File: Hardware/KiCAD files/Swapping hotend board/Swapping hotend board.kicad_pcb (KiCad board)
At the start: 2 copper layers, 3 parts, among them J19 PINHD_1x10_Male, J24 JST_SMD_1.0mm_Vertical

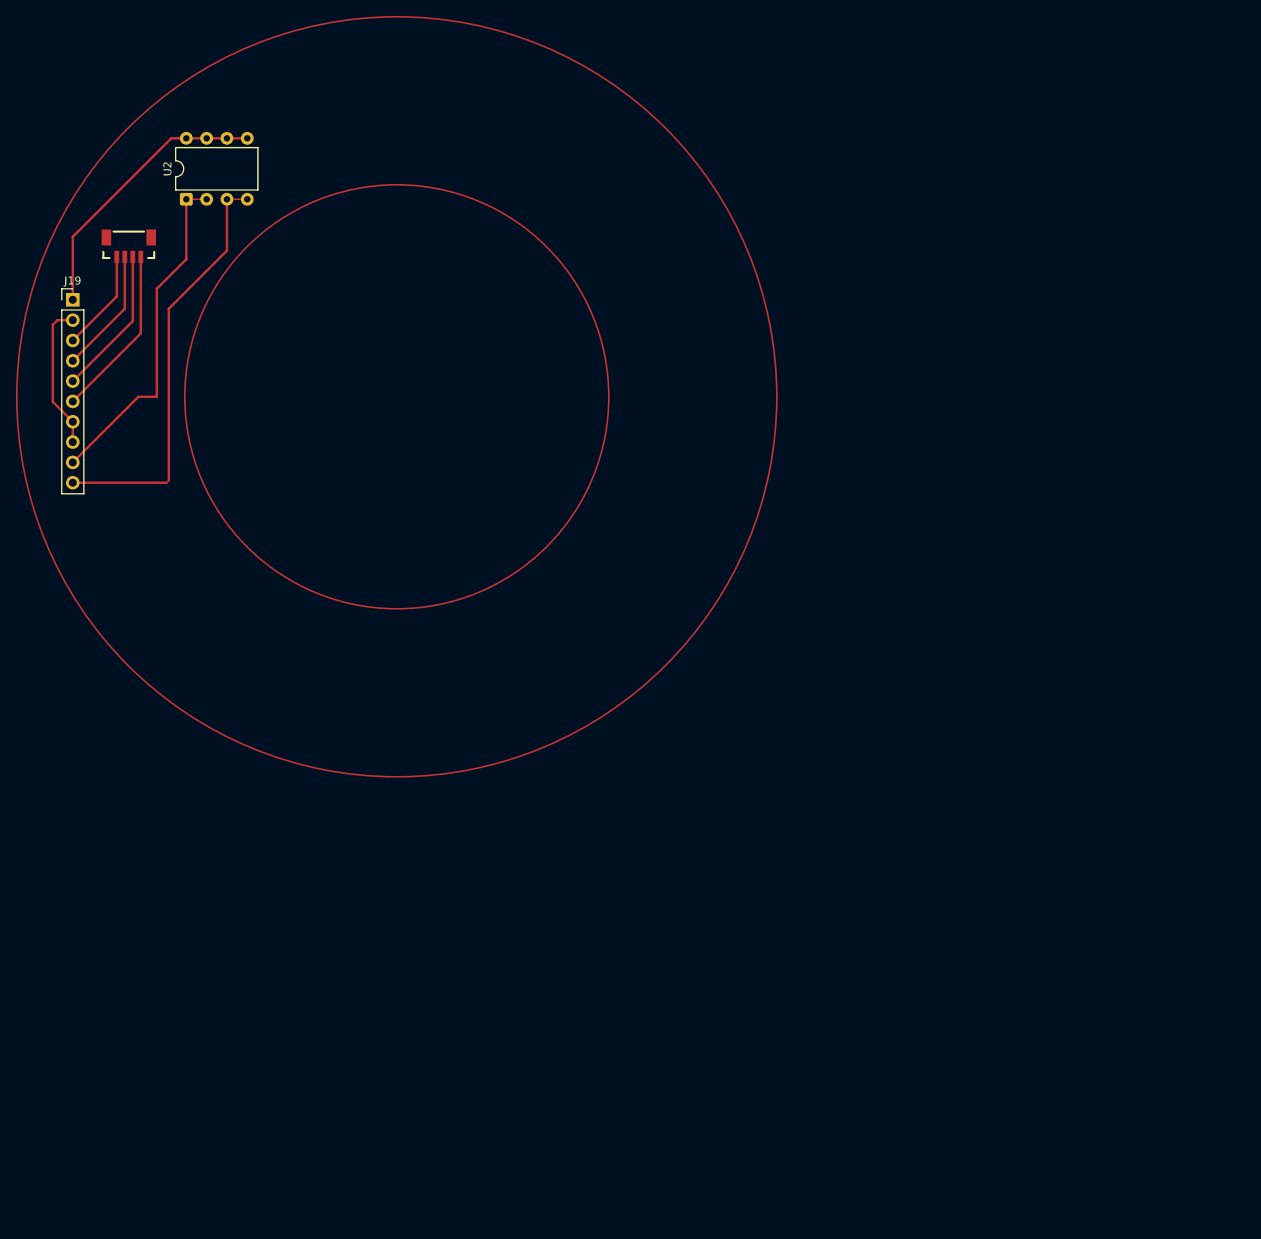
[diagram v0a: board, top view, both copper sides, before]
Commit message: Hotfix to create non-swapping board
hotfix on non-swapping done, swapping board is mapped for completion after CAD modeling phase begins
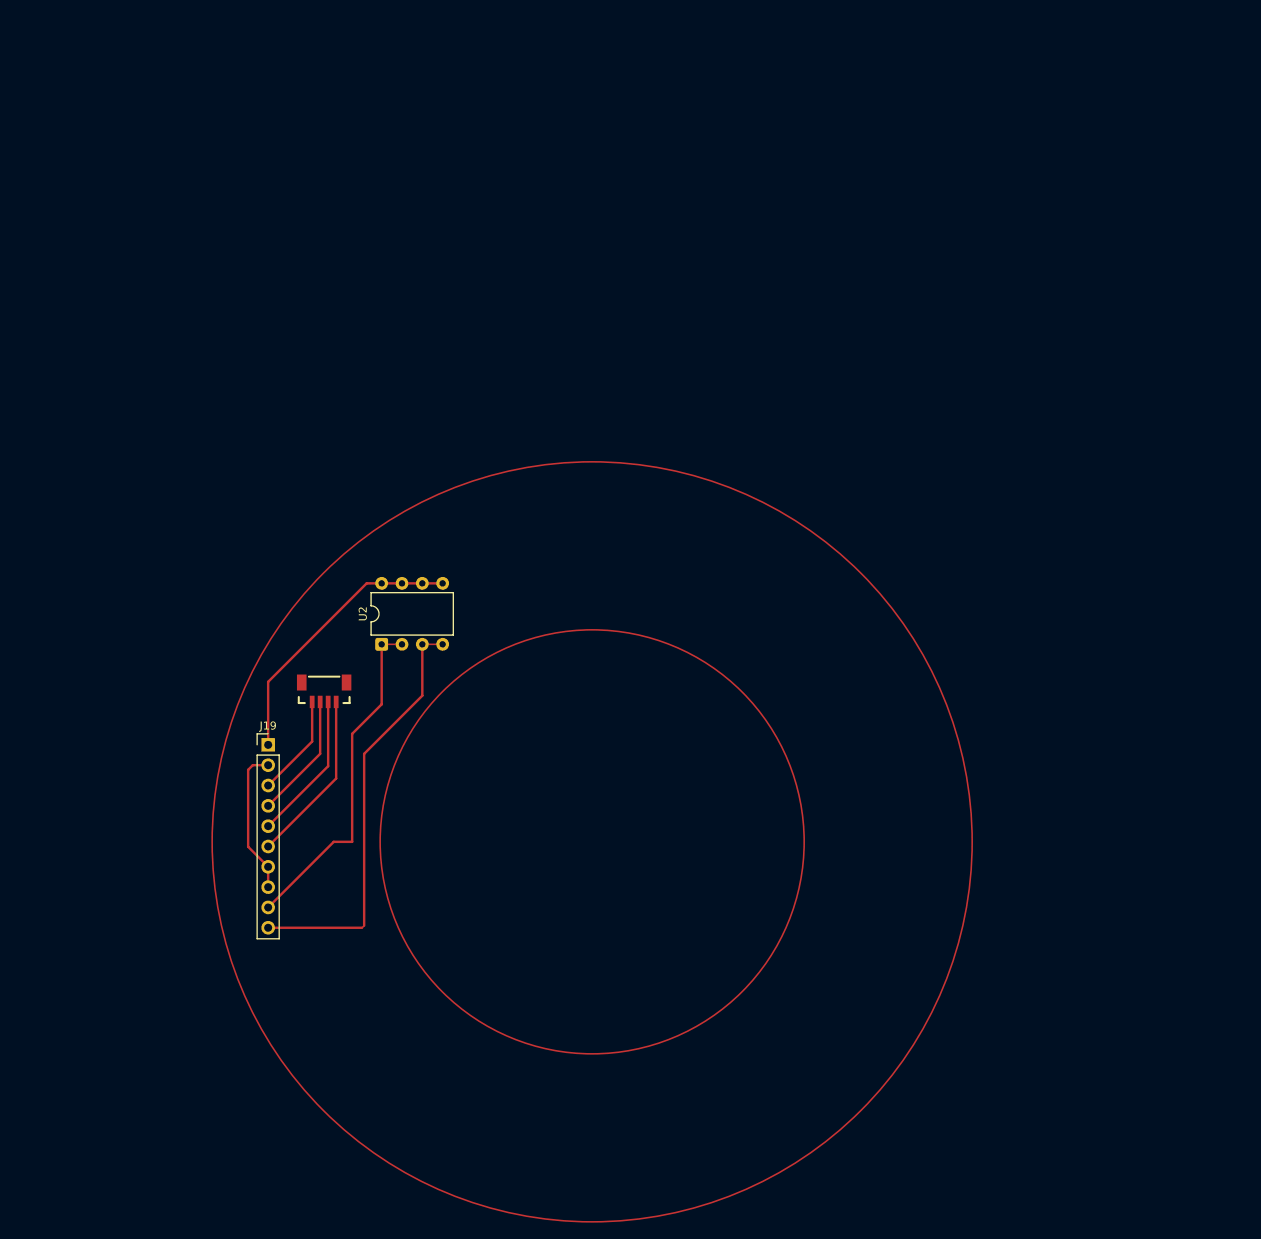
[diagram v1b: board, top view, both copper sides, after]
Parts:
- moved J19 60.8 mm to (46.4, 91.0)
- moved J24 60.8 mm to (53.4, 84.1)
- moved U2 60.8 mm to (60.6, 78.4)
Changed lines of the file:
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@@
 		(capping no)
 		(filling no)
-		(zone_defaults)
 		(pcbplotparams
 			(layerselection 0x00000000_00000000_55555555_5755f5ff)
@@
 	(footprint "Package_DIP:DIP-8_W7.62mm"
 		(layer "F.Cu")
-		(at 36.19 22.81 90)
+		(at 60.61 78.44 90)
 		(descr "8-lead though-hole mounted DIP package, row spacing 7.62mm (300 mils)")
 		(tags "THT DIP DIL PDIP 2.54mm 7.62mm 300mil")
@@
 		)
 		(point
-			(at 40 19)
+			(at 64.42 74.63)
 			(size 1.27)
 			(layer "F.Fab")
@@
 	(footprint "PCM_SparkFun-Connector:JST_1x04_P1.0mm_Vertical_SMD"
 		(layer "F.Cu")
-		(at 29 28.5)
+		(at 53.42 84.13)
 		(tags "SparkFun Qwiic Connector")
 		(property "Reference" "J24"
@@
 	(footprint "Connector_PinHeader_2.54mm:PinHeader_1x10_P2.54mm_Vertical"
 		(layer "F.Cu")
-		(at 22 35.38)
+		(at 46.42 91.01)
 		(descr "Through hole straight pin header, 1x10, 2.54mm pitch, single row")
 		(tags "Through hole pin header THT 1x10 2.54mm single row")
@@
 	)
 	(gr_circle
-		(center 62.5 47.5)
-		(end 89 47.31)
+		(center 86.92 103.13)
+		(end 113.42 102.94)
 		(stroke
 			(width 0.2)
@@
 	)
 	(gr_circle
-		(center 62.5 47.5)
-		(end 110 47.31)
+		(center 86.92 103.13)
+		(end 134.42 102.94)
 		(stroke
 			(width 0.2)
@@
 		(layer "F.Cu")
 		(pts
-			(xy 62.5 47.5) (xy 89.000681 47.5)
+			(xy 86.92 103.13) (xy 113.420681 103.13)
 		)
 		(height -51)
@@
 		)
 		(gr_text "26.5007"
-			(at 75.750341 -5.3 0)
+			(at 100.170341 50.33 0)
 			(layer "F.Cu")
 			(effects
@@
 		(layer "F.Cu")
 		(pts
-			(xy 62.5 47.5) (xy 110.00038 47.5)
+			(xy 86.92 103.13) (xy 134.42038 103.13)
 		)
 		(height -58.5)
@@
 		)
 		(gr_text "47.5004"
-			(at 86.25019 -12.8 0)
+			(at 110.67019 42.83 0)
 			(layer "F.Cu")
 			(effects
@@
 	)
 	(segment
-		(start 41.27 22.81)
-		(end 41.27 29.23)
+		(start 56.92 89.63)
+		(end 56.92 103.13)
+		(width 0.3048)
+		(layer "F.Cu")
+		(net "Net-(U2-SW1-P1)")
+	)
+	(segment
+		(start 60.61 78.44)
+		(end 60.61 85.94)
+		(width 0.3048)
+		(layer "F.Cu")
+		(net "Net-(U2-SW1-P1)")
+	)
+	(segment
+		(start 63.15 78.44)
+		(end 60.61 78.44)
+		(width 0.2)
+		(layer "F.Cu")
+		(net "Net-(U2-SW1-P1)")
+	)
+	(segment
+		(start 54.62 103.13)
+		(end 46.42 111.33)
+		(width 0.3048)
+		(layer "F.Cu")
+		(net "Net-(U2-SW1-P1)")
+	)
+	(segment
+		(start 60.61 85.94)
+		(end 56.92 89.63)
+		(width 0.3048)
+		(layer "F.Cu")
+		(net "Net-(U2-SW1-P1)")
+	)
+	(segment
+		(start 56.92 103.13)
+		(end 54.62 103.13)
+		(width 0.3048)
+		(layer "F.Cu")
+		(net "Net-(U2-SW1-P1)")
+	)
+	(segment
+		(start 65.69 78.44)
+		(end 65.69 84.86)
 		(width 0.3048)
 		(layer "F.Cu")
@@
 	)
 	(segment
-		(start 34 36.5)
-		(end 34 57.98)
+		(start 58.42 92.13)
+		(end 58.42 113.61)
 		(width 0.3048)
 		(layer "F.Cu")
@@
 	)
 	(segment
-		(start 34 57.98)
-		(end 33.74 58.24)
+		(start 58.42 113.61)
+		(end 58.16 113.87)
 		(width 0.2)
 		(layer "F.Cu")
@@
 	)
 	(segment
-		(start 43.81 22.81)
-		(end 41.27 22.81)
+		(start 68.23 78.44)
+		(end 65.69 78.44)
 		(width 0.2)
 		(layer "F.Cu")
@@
 	)
 	(segment
-		(start 41.27 29.23)
-		(end 34 36.5)
+		(start 65.69 84.86)
+		(end 58.42 92.13)
 		(width 0.3048)
 		(layer "F.Cu")
@@
 	)
 	(segment
-		(start 33.74 58.24)
-		(end 22 58.24)
+		(start 58.16 113.87)
+		(end 46.42 113.87)
 		(width 0.3048)
 		(layer "F.Cu")
@@
 	)
 	(segment
-		(start 28.5 36.5)
-		(end 22 43)
+		(start 65.69 70.82)
+		(end 68.23 70.82)
+		(width 0.3048)
+		(layer "F.Cu")
+		(net "Net-(U2-SW1-P1-input)")
+	)
+	(segment
+		(start 63.15 70.82)
+		(end 60.61 70.82)
+		(width 0.3048)
+		(layer "F.Cu")
+		(net "Net-(U2-SW1-P1-input)")
+	)
+	(segment
+		(start 46.42 83.13)
+		(end 46.42 91.01)
+		(width 0.3048)
+		(layer "F.Cu")
+		(net "Net-(U2-SW1-P1-input)")
+	)
+	(segment
+		(start 59.23 70.82)
+		(end 58.73 70.82)
+		(width 0.2)
+		(layer "F.Cu")
+		(net "Net-(U2-SW1-P1-input)")
+	)
+	(segment
+		(start 65.69 70.82)
+		(end 63.15 70.82)
+		(width 0.3048)
+		(layer "F.Cu")
+		(net "Net-(U2-SW1-P1-input)")
+	)
+	(segment
+		(start 60.61 70.82)
+		(end 58.73 70.82)
+		(width 0.3048)
+		(layer "F.Cu")
+		(net "Net-(U2-SW1-P1-input)")
+	)
+	(segment
+		(start 58.73 70.82)
+		(end 46.42 83.13)
+		(width 0.3048)
+		(layer "F.Cu")
+		(net "Net-(U2-SW1-P1-input)")
+	)
+	(segment
+		(start 51.92 85.641)
+		(end 51.92 90.59)
+		(width 0.3048)
+		(layer "F.Cu")
+		(net "Net-(J24-Pin_1)")
+	)
+	(segment
+		(start 51.92 90.59)
+		(end 46.42 96.09)
+		(width 0.3048)
+		(layer "F.Cu")
+		(net "Net-(J24-Pin_1)")
+	)
+	(segment
+		(start 52.92 92.13)
+		(end 46.42 98.63)
 		(width 0.3048)
 		(layer "F.Cu")
@@
 	)
 	(segment
-		(start 28.5 30.011)
-		(end 28.5 36.5)
+		(start 52.92 85.641)
+		(end 52.92 92.13)
 		(width 0.3048)
 		(layer "F.Cu")
@@
 	)
 	(segment
-		(start 22 50.62)
-		(end 19.5 48.12)
+		(start 53.92 93.67)
+		(end 46.42 101.17)
+		(width 0.3048)
+		(layer "F.Cu")
+		(net "Net-(J24-Pin_3)")
+	)
+	(segment
+		(start 53.92 85.641)
+		(end 53.92 93.67)
+		(width 0.3048)
+		(layer "F.Cu")
+		(net "Net-(J24-Pin_3)")
+	)
+	(segment
+		(start 54.92 95.21)
+		(end 46.42 103.71)
+		(width 0.3048)
+		(layer "F.Cu")
+		(net "Net-(J24-Pin_4)")
+	)
+	(segment
+		(start 54.92 85.641)
+		(end 54.92 95.21)
+		(width 0.3048)
+		(layer "F.Cu")
+		(net "Net-(J24-Pin_4)")
+	)
+	(segment
+		(start 46.42 106.25)
+		(end 43.92 103.75)
 		(width 0.3048)
 		(layer "F.Cu")
@@
 	)
 	(segment
-		(start 19.5 38.5)
-		(end 20.08 37.92)
+		(start 43.92 94.13)
+		(end 44.5 93.55)
 		(width 0.3048)
 		(layer "F.Cu")
@@
 	)
 	(segment
-		(start 19.5 48.12)
-		(end 19.5 38.5)
+		(start 43.92 103.75)
+		(end 43.92 94.13)
 		(width 0.3048)
 		(layer "F.Cu")
@@
 	)
 	(segment
-		(start 22 53.16)
-		(end 22 50.62)
+		(start 46.42 108.79)
+		(end 46.42 106.25)
 		(width 0.3048)
 		(layer "F.Cu")
@@
 	)
 	(segment
-		(start 20.08 37.92)
-		(end 22 37.92)
+		(start 44.5 93.55)
+		(end 46.42 93.55)
 		(width 0.3048)
 		(layer "F.Cu")
 		(net "GND")
 	)
-	(segment
-		(start 41.27 15.19)
-		(end 43.81 15.19)
-		(width 0.3048)
-		(layer "F.Cu")
-		(net "Net-(U2-SW1-P1-input)")
-	)
-	(segment
-		(start 38.73 15.19)
-		(end 36.19 15.19)
-		(width 0.3048)
-		(layer "F.Cu")
-		(net "Net-(U2-SW1-P1-input)")
-	)
-	(segment
-		(start 22 27.5)
-		(end 22 35.38)
-		(width 0.3048)
-		(layer "F.Cu")
-		(net "Net-(U2-SW1-P1-input)")
-	)
-	(segment
-		(start 34.81 15.19)
-		(end 34.31 15.19)
-		(width 0.2)
-		(layer "F.Cu")
-		(net "Net-(U2-SW1-P1-input)")
-	)
-	(segment
-		(start 41.27 15.19)
-		(end 38.73 15.19)
-		(width 0.3048)
-		(layer "F.Cu")
-		(net "Net-(U2-SW1-P1-input)")
-	)
-	(segment
-		(start 36.19 15.19)
-		(end 34.31 15.19)
-		(width 0.3048)
-		(layer "F.Cu")
-		(net "Net-(U2-SW1-P1-input)")
-	)
-	(segment
-		(start 34.31 15.19)
-		(end 22 27.5)
-		(width 0.3048)
-		(layer "F.Cu")
-		(net "Net-(U2-SW1-P1-input)")
-	)
-	(segment
-		(start 32.5 34)
-		(end 32.5 47.5)
-		(width 0.3048)
-		(layer "F.Cu")
-		(net "Net-(U2-SW1-P1)")
-	)
-	(segment
-		(start 36.19 22.81)
-		(end 36.19 30.31)
-		(width 0.3048)
-		(layer "F.Cu")
-		(net "Net-(U2-SW1-P1)")
-	)
-	(segment
-		(start 38.73 22.81)
-		(end 36.19 22.81)
-		(width 0.2)
-		(layer "F.Cu")
-		(net "Net-(U2-SW1-P1)")
-	)
-	(segment
-		(start 30.2 47.5)
-		(end 22 55.7)
-		(width 0.3048)
-		(layer "F.Cu")
-		(net "Net-(U2-SW1-P1)")
-	)
-	(segment
-		(start 36.19 30.31)
-		(end 32.5 34)
-		(width 0.3048)
-		(layer "F.Cu")
-		(net "Net-(U2-SW1-P1)")
-	)
-	(segment
-		(start 32.5 47.5)
-		(end 30.2 47.5)
-		(width 0.3048)
-		(layer "F.Cu")
-		(net "Net-(U2-SW1-P1)")
-	)
-	(segment
-		(start 27.5 30.011)
-		(end 27.5 34.96)
-		(width 0.3048)
-		(layer "F.Cu")
-		(net "Net-(J24-Pin_1)")
-	)
-	(segment
-		(start 27.5 34.96)
-		(end 22 40.46)
-		(width 0.3048)
-		(layer "F.Cu")
-		(net "Net-(J24-Pin_1)")
-	)
-	(segment
-		(start 30.5 39.58)
-		(end 22 48.08)
-		(width 0.3048)
-		(layer "F.Cu")
-		(net "Net-(J24-Pin_4)")
-	)
-	(segment
-		(start 30.5 30.011)
-		(end 30.5 39.58)
-		(width 0.3048)
-		(layer "F.Cu")
-		(net "Net-(J24-Pin_4)")
-	)
-	(segment
-		(start 29.5 38.04)
-		(end 22 45.54)
-		(width 0.3048)
-		(layer "F.Cu")
-		(net "Net-(J24-Pin_3)")
-	)
-	(segment
-		(start 29.5 30.011)
-		(end 29.5 38.04)
-		(width 0.3048)
-		(layer "F.Cu")
-		(net "Net-(J24-Pin_3)")
-	)
 	(embedded_fonts no)

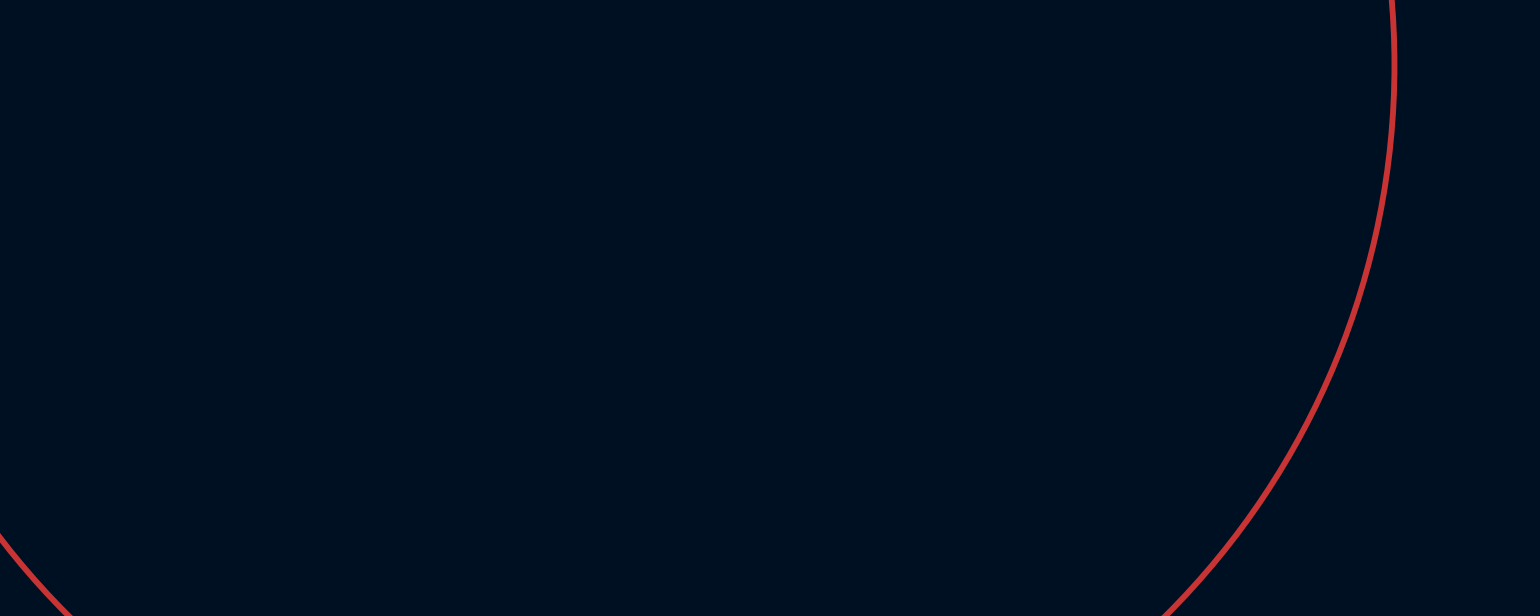
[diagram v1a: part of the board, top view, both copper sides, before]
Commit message: 1st push of PCB's for printing
This is pre-peer review. This almost certainly has section that need adjustment. also realized I'm missing the USB-Uart bridge. first thing added in next version.
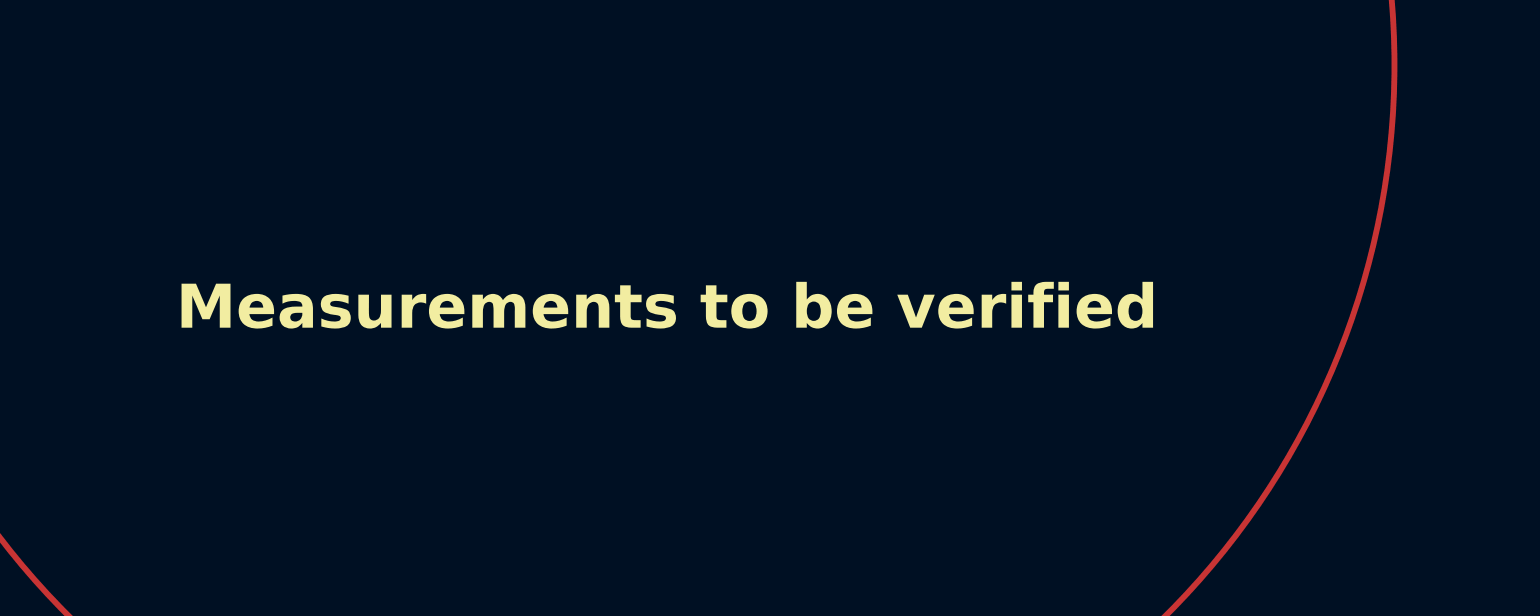
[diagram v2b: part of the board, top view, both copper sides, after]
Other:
- board text added: "Measurements to be verified"
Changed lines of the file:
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@@
 		(layer "F.Cu")
+	)
+	(gr_text "Measurements to be verified"
+		(at 71.882 112.268 0)
+		(layer "F.SilkS")
+		(effects
+			(font
+				(size 1.5 1.5)
+				(thickness 0.3)
+				(bold yes)
+			)
+			(justify left bottom)
+		)
 	)
 	(dimension
